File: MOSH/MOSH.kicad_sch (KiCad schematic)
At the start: 11 parts, among them J1 Power, J2 Digital/PWM, J3 Analog, J4 Digital/PWM, U1 LTC1050

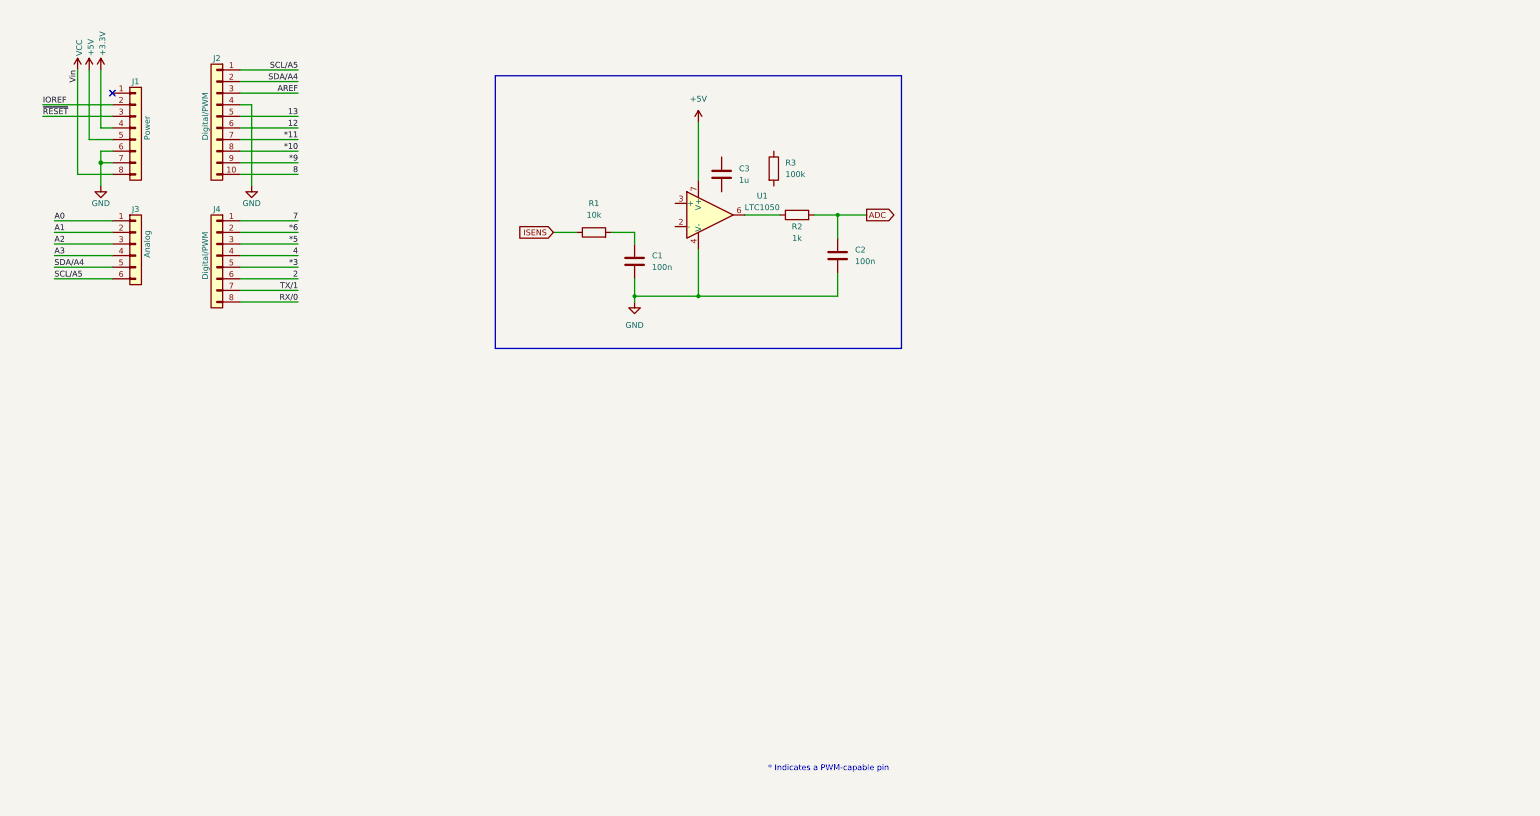
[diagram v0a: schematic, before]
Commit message: pcb schematic transimpedance amplifier, variable resistance, lora board and gas sensor
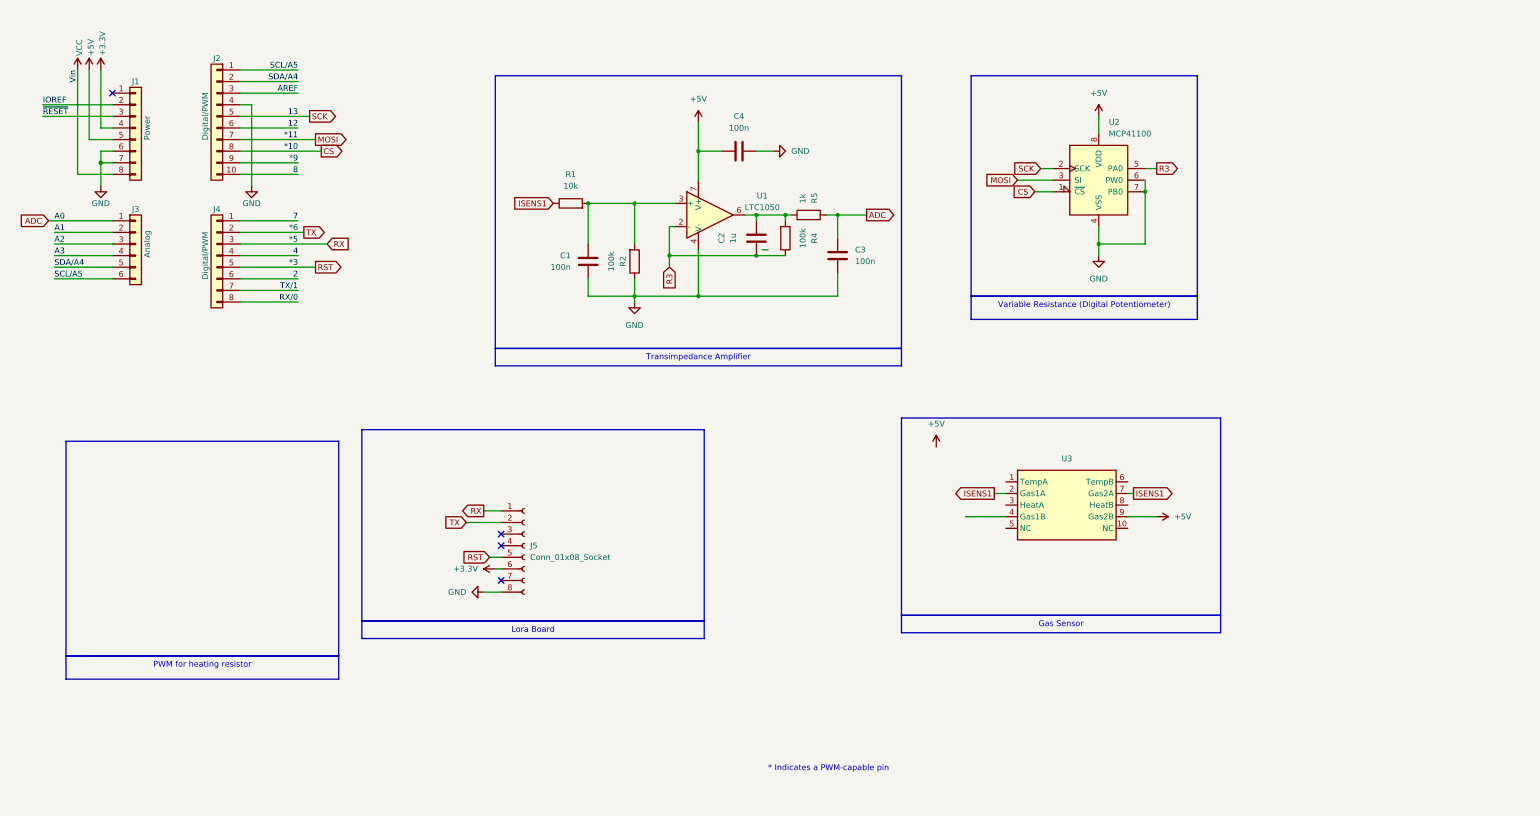
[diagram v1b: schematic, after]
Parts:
- removed R3: 100k, symbol Device:R
- added C4: 100n, symbol Device:C
- added J5: Conn_01x08_Socket, Connector_PinSocket_2.54mm:PinSocket_1x08_P2.54mm_Horizontal, symbol Connector:Conn_01x08_Socket
- added R4: 100k, symbol Device:R
- added R5: 1k, symbol Device:R
- added U2: MCP41100, symbol Potentiometer_Digital:MCP41100
- added U3: ~, Package_TO_SOT_THT:TO-5-10, symbol Library_AJB_RM_0:Gas_Sensor
- R2: value 1k -> 100k
- renumbered C3 to C2, C2 to C3
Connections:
- net A0 is gone; now on net ADC: J3.1 (Pin_1)
- net +5V: now also C4.1, U2.8 (VDD), U3.9 (Gas2B)
- net ADC: now also R5.2; no longer R2.2
- net GND: now also R2.1, C4.2, J5.8 (Pin_8), U2.4 (VSS), U2.6 (PW0), U2.7 (PB0)
- net R3: now reaches U1.2 (-)
- net R3: now also C2.1, R4.1, U2.5 (PA0)
- net at U1.3 (+): now also C1.2, R1.2, R2.2
- net at U1.6: now also C2.2, R4.2, R5.1; no longer R2.1
- net *10 renamed CS
- net CS: now also U2.1 (~{CS})
- net *11 renamed MOSI
- net MOSI: now also U2.3 (SI)
- net *3 renamed RST
- net RST: now also J5.5 (Pin_5)
- net *5 renamed RX
- net RX: now also J5.1 (Pin_1)
- net *6 renamed TX
- net TX: now also J5.2 (Pin_2)
- net 13 renamed SCK
- net SCK: now also U2.2 (SCK)
- net ISENS renamed ISENS1
- net ISENS1: now also U3.2 (Gas1A), U3.7 (Gas2A)
- new net +3.3V: J5.6 (Pin_6)
- no-connect marks 1 -> 4
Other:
- title: (none) -> ISS 2023 AJB & RM - Gas Sensor
- moved on the sheet: C1, C2, R1, R2

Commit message: pcb schematic fini
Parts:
- added C5: 100n, symbol Device:C
- added J6: Conn_01x03_Pin, Connector_PinHeader_2.54mm:PinHeader_1x03_P2.54mm_Vertical, symbol Connector:Conn_01x03_Pin
- added Q1: IRF540N, Package_TO_SOT_THT:TO-220-3_Vertical, symbol Transistor_FET:IRF540N
- added R6: 100k, symbol Device:R
- added R7: 10k, symbol Device:R
- added R8: 1k, symbol Device:R
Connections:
- net 2 is gone; now on net RX: J4.6 (Pin_6)
- net 4 is gone; now on net RST: J4.4 (Pin_4)
- net A1 is gone; now on net VTEMP: J3.2 (Pin_2)
- net +5V: now also U3.4 (Gas1B), R6.1
- net GND: now also U3.6 (TempB), U3.8 (HeatB), C5.2, Q1.3 (S)
- net ISENS1: now also J6.1 (Pin_1); no longer R1.1, U3.7 (Gas2A)
- net RST: no longer J4.5 (Pin_5)
- net RX: no longer J4.3 (Pin_3)
- net TX: now also J4.5 (Pin_5); no longer J4.2 (Pin_2)
- net VCC: now also C5.1, R7.1
- net VTEMP: now reaches U3.1 (TempA)
- net VTEMP: now also R6.2
- net VHEAT: now reaches U3.3 (HeatA)
- net VHEAT: now also Q1.2 (D), R7.2
- new net: J6.2 (Pin_2), R1.1
- new net: Q1.1 (G), R8.2
- new net *5: J4.3 (Pin_3)
- new net ISENS2: J6.3 (Pin_3), U3.7 (Gas2A)
- new net PWM: J4.2 (Pin_2), R8.1
- no-connect marks 4 -> 6

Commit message: add all footprints and start rooting
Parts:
- added C6: 100n, Capacitor_THT:C_Disc_D4.7mm_W2.5mm_P5.00mm, symbol Device:C
- C1, C3, C4, C5: footprint (none) -> Capacitor_THT:C_Disc_D4.7mm_W2.5mm_P5.00mm
- C2: footprint (none) -> Capacitor_THT:C_Rect_L7.0mm_W4.5mm_P5.00mm
- J5: footprint Connector_PinSocket_2.54mm:PinSocket_1x08_P2.54mm_Horizontal -> Connector_PinSocket_2.54mm:PinSocket_1x08_P2.54mm_Vertical
- R1, R2, R4, R5, R6, R7, R8: footprint (none) -> Resistor_THT:R_Axial_DIN0207_L6.3mm_D2.5mm_P10.16mm_Horizontal
- U2: footprint (none) -> Package_DIP:DIP-8_W7.62mm
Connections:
- net +3V3 is gone; now on net +3.3V: J1.4 (Pin_4)
- net +3.3V: now also C6.1
- net GND: now also C6.2
- no-connect marks 6 -> 23

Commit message: presque fini routage il manque plus que quelques détails ; penser à checker les règles electrique
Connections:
- net ISENS2: now also U3.5 (NC)
- no-connect marks 23 -> 22
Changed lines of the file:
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@@
   (junction (at 175.26 67.31) (diameter 0) (color 0 0 0 0)
   )
-  (no_connect (at 229.87 127))
   (no_connect (at 74.93 46.99))
   (no_connect (at 119.38 138.43))
@@
     )
   )
+  (global_label "ISENS2" (shape output) (at 229.87 127 180) (fields_autoplaced)
+    (effects (font (size 1.27 1.27)) (justify right))
+    (property "Intersheetrefs" "${INTERSHEET_REFS}" (at 220.0769 127 0)
+      (effects (font (size 1.27 1.27)) (justify right) hide)
+    )
+  )
